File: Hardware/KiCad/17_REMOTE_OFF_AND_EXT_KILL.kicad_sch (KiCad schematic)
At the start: 0 parts

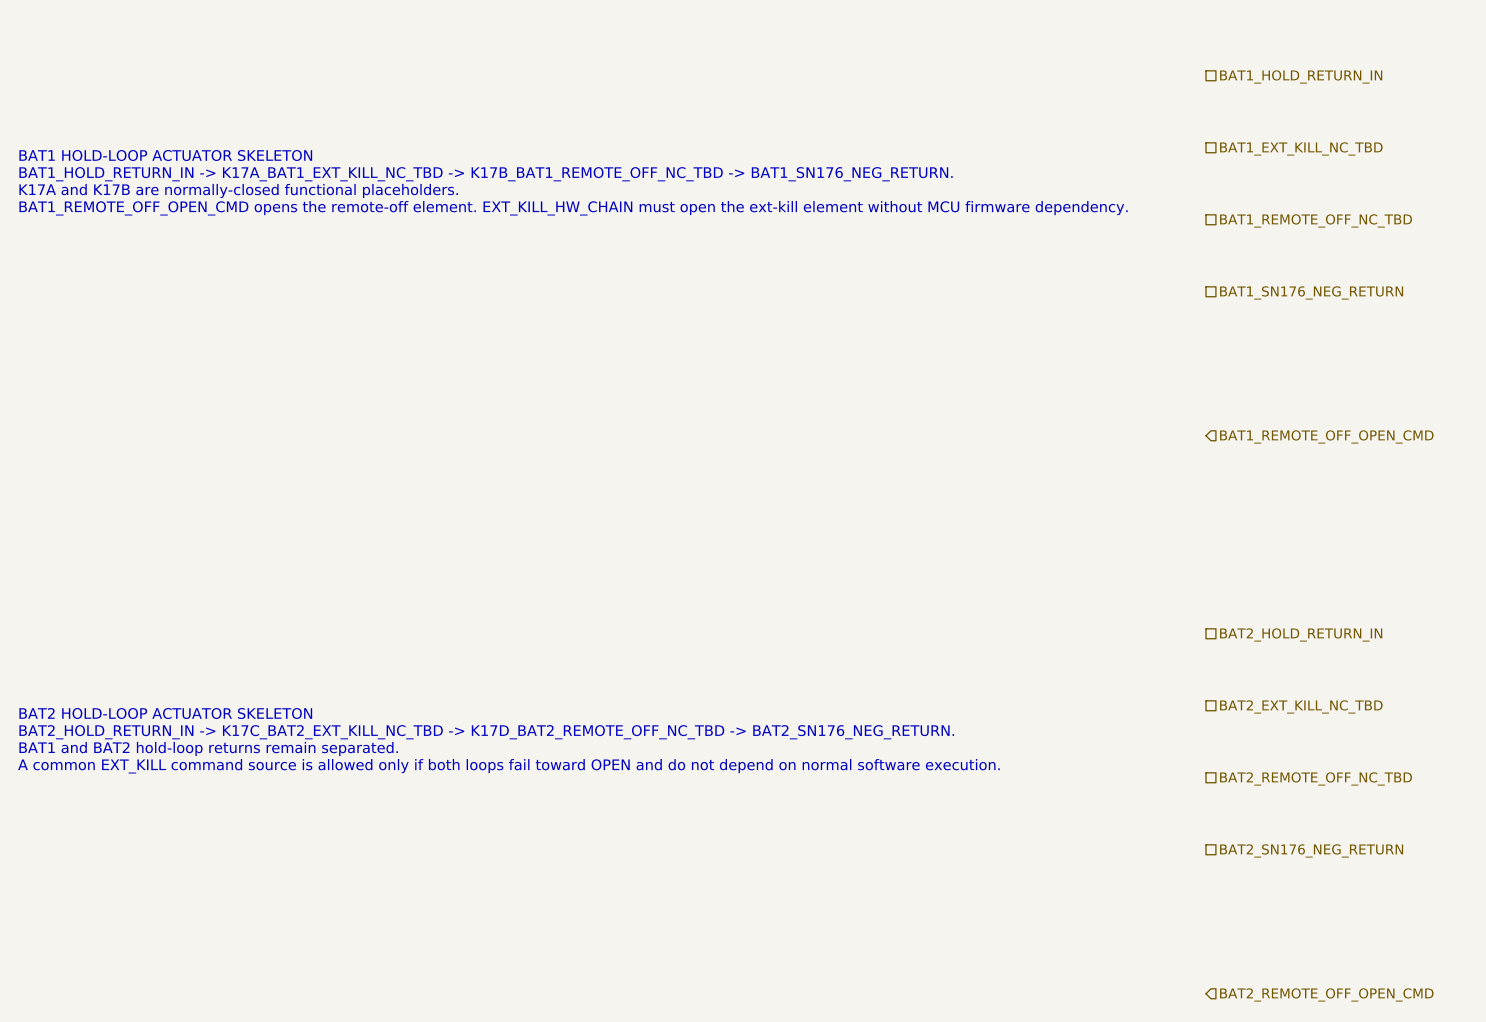
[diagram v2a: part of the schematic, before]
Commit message: hardware: align hold-loop returns to battery negative nets
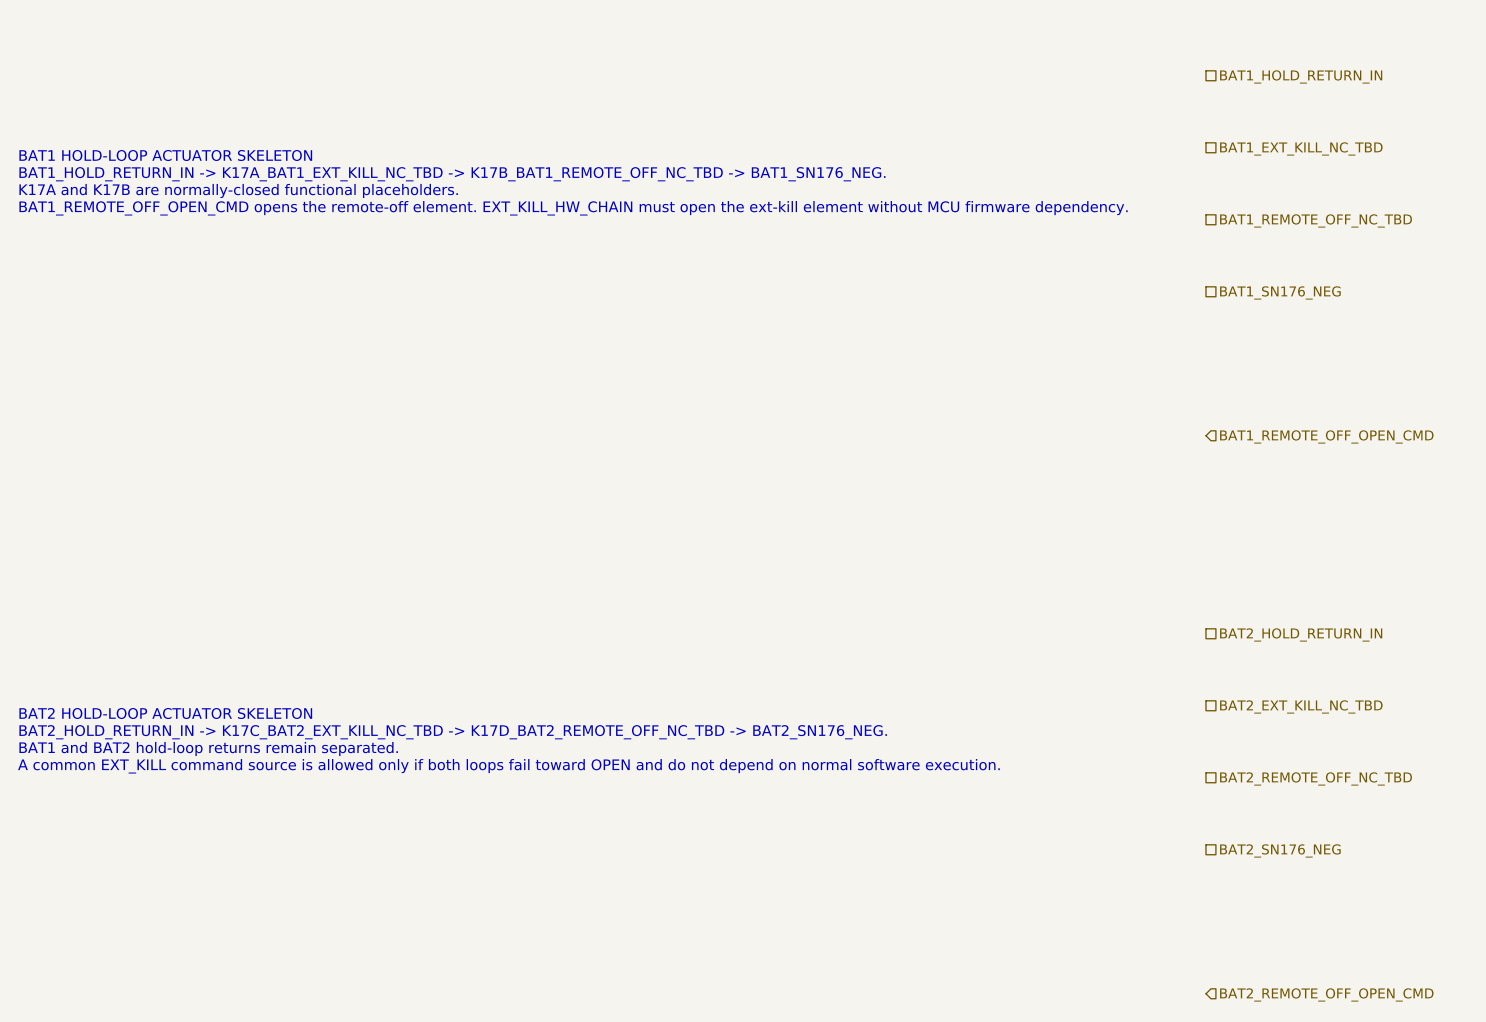
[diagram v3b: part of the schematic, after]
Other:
- note added: "BAT1 HOLD-LOOP ACTUATOR SKELETON BAT1_HOLD_RETURN_IN -> K17A_BAT1_EXT_KILL_NC_TBD -> K17B_BAT1_REMOTE_OFF_NC_TBD -> BAT1_SN176_NEG. K17A and K17B are normally-closed functional placeholders. BAT1_REMOTE_OFF_OPEN_CMD opens the remote-off element. EXT_KILL_HW_CHAIN must open the ext-kill element without MCU firmware dependency."
- note added: "BAT2 HOLD-LOOP ACTUATOR SKELETON BAT2_HOLD_RETURN_IN -> K17C_BAT2_EXT_KILL_NC_TBD -> K17D_BAT2_REMOTE_OFF_NC_TBD -> BAT2_SN176_NEG. BAT1 and BAT2 hold-loop returns remain separated. A common EXT_KILL command source is allowed only if both loops fail toward OPEN and do not depend on normal software execution."
- note removed: "BAT1 HOLD-LOOP ACTUATOR SKELETON BAT1_HOLD_RETURN_IN -> K17A_BAT1_EXT_KILL_NC_TBD -> K17B_BAT1_REMOTE_OFF_NC_TBD -> BAT1_SN176_NEG_RETURN. K17A and K17B are normally-closed functional placeholders. BAT1_REMOTE_OFF_OPEN_CMD opens the remote-off element. EXT_KILL_HW_CHAIN must open the ext-kill element without MCU firmware dependency."
- note removed: "BAT2 HOLD-LOOP ACTUATOR SKELETON BAT2_HOLD_RETURN_IN -> K17C_BAT2_EXT_KILL_NC_TBD -> K17D_BAT2_REMOTE_OFF_NC_TBD -> BAT2_SN176_NEG_RETURN. BAT1 and BAT2 hold-loop returns remain separated. A common EXT_KILL command source is allowed only if both loops fail toward OPEN and do not depend on normal software execution."
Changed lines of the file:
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@@
 		(title "17_REMOTE_OFF_AND_EXT_KILL - hold-loop final actuators")
 		(date "2026-07-15")
-		(rev "C0")
+		(rev "C1")
 		(company "Gonoboben/plataVM")
-		(comment 1 "Symbol skeleton: NC actuator placement zones for K_BATx hold-loop interruption")
+		(comment 1 "Interface consistency: NC actuator zones and exact hold-loop return nets")
 		(comment 2 "Text-only placeholders; no relay, MOSFET, optocoupler or driver topology selected")
 	)
@@
 		(uuid "bfe-symbol-00000017-0000-4000-8000-000000000101")
 	)
-	(text "BAT1 HOLD-LOOP ACTUATOR SKELETON\nBAT1_HOLD_RETURN_IN -> K17A_BAT1_EXT_KILL_NC_TBD -> K17B_BAT1_REMOTE_OFF_NC_TBD -> BAT1_SN176_NEG_RETURN.\nK17A and K17B are normally-closed functional placeholders.\nBAT1_REMOTE_OFF_OPEN_CMD opens the remote-off element. EXT_KILL_HW_CHAIN must open the ext-kill element without MCU firmware dependency."
+	(text "BAT1 HOLD-LOOP ACTUATOR SKELETON\nBAT1_HOLD_RETURN_IN -> K17A_BAT1_EXT_KILL_NC_TBD -> K17B_BAT1_REMOTE_OFF_NC_TBD -> BAT1_SN176_NEG.\nK17A and K17B are normally-closed functional placeholders.\nBAT1_REMOTE_OFF_OPEN_CMD opens the remote-off element. EXT_KILL_HW_CHAIN must open the ext-kill element without MCU firmware dependency."
 		(exclude_from_sim no)
 		(at 12 66 0)
@@
 		(uuid "bfe-symbol-00000017-0000-4000-8000-000000000102")
 	)
-	(text "BAT2 HOLD-LOOP ACTUATOR SKELETON\nBAT2_HOLD_RETURN_IN -> K17C_BAT2_EXT_KILL_NC_TBD -> K17D_BAT2_REMOTE_OFF_NC_TBD -> BAT2_SN176_NEG_RETURN.\nBAT1 and BAT2 hold-loop returns remain separated.\nA common EXT_KILL command source is allowed only if both loops fail toward OPEN and do not depend on normal software execution."
+	(text "BAT2 HOLD-LOOP ACTUATOR SKELETON\nBAT2_HOLD_RETURN_IN -> K17C_BAT2_EXT_KILL_NC_TBD -> K17D_BAT2_REMOTE_OFF_NC_TBD -> BAT2_SN176_NEG.\nBAT1 and BAT2 hold-loop returns remain separated.\nA common EXT_KILL command source is allowed only if both loops fail toward OPEN and do not depend on normal software execution."
 		(exclude_from_sim no)
 		(at 12 128 0)
@@
 	(hierarchical_label "BAT1_EXT_KILL_NC_TBD" (shape passive) (exclude_from_sim no) (at 144 62 0) (effects (font (size 1.1 1.1)) (justify left)) (uuid "bfe-symbol-00000017-0000-4000-8000-000000000202"))
 	(hierarchical_label "BAT1_REMOTE_OFF_NC_TBD" (shape passive) (exclude_from_sim no) (at 144 70 0) (effects (font (size 1.1 1.1)) (justify left)) (uuid "bfe-symbol-00000017-0000-4000-8000-000000000203"))
-	(hierarchical_label "BAT1_SN176_NEG_RETURN" (shape passive) (exclude_from_sim no) (at 144 78 0) (effects (font (size 1.1 1.1)) (justify left)) (uuid "bfe-symbol-00000017-0000-4000-8000-000000000204"))
+	(hierarchical_label "BAT1_SN176_NEG" (shape passive) (exclude_from_sim no) (at 144 78 0) (effects (font (size 1.1 1.1)) (justify left)) (uuid "bfe-symbol-00000017-0000-4000-8000-000000000204"))
 	(hierarchical_label "BAT2_HOLD_RETURN_IN" (shape passive) (exclude_from_sim no) (at 144 116 0) (effects (font (size 1.1 1.1)) (justify left)) (uuid "bfe-symbol-00000017-0000-4000-8000-000000000205"))
 	(hierarchical_label "BAT2_EXT_KILL_NC_TBD" (shape passive) (exclude_from_sim no) (at 144 124 0) (effects (font (size 1.1 1.1)) (justify left)) (uuid "bfe-symbol-00000017-0000-4000-8000-000000000206"))
 	(hierarchical_label "BAT2_REMOTE_OFF_NC_TBD" (shape passive) (exclude_from_sim no) (at 144 132 0) (effects (font (size 1.1 1.1)) (justify left)) (uuid "bfe-symbol-00000017-0000-4000-8000-000000000207"))
-	(hierarchical_label "BAT2_SN176_NEG_RETURN" (shape passive) (exclude_from_sim no) (at 144 140 0) (effects (font (size 1.1 1.1)) (justify left)) (uuid "bfe-symbol-00000017-0000-4000-8000-000000000208"))
+	(hierarchical_label "BAT2_SN176_NEG" (shape passive) (exclude_from_sim no) (at 144 140 0) (effects (font (size 1.1 1.1)) (justify left)) (uuid "bfe-symbol-00000017-0000-4000-8000-000000000208"))
 	(hierarchical_label "BAT1_REMOTE_OFF_OPEN_CMD" (shape input) (exclude_from_sim no) (at 144 94 0) (effects (font (size 1.1 1.1)) (justify left)) (uuid "bfe-symbol-00000017-0000-4000-8000-000000000209"))
 	(hierarchical_label "BAT2_REMOTE_OFF_OPEN_CMD" (shape input) (exclude_from_sim no) (at 144 156 0) (effects (font (size 1.1 1.1)) (justify left)) (uuid "bfe-symbol-00000017-0000-4000-8000-000000000210"))
